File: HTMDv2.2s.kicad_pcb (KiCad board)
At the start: 2 copper layers, 90 x 49.9 mm, 105 parts, among them IC1 TJA1441AT_0Z, IC2 A3921KLPTR-T, IC3 TMP275AQDGKRQ1, J1 Conn_01x04, J10 Conn_01x02, J11 Conn_01x02, J2 Conn_01x04, J3 Conn_01x06, J4 Conn_01x01, J5 Conn_01x01_Pin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

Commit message: update
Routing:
- net SPI_SCK: track 7.98 -> 0.00 mm
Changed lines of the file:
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@@
   (segment (start 129.7262 74.1172) (end 128.6267 74.1172) (width 0.25) (layer "F.Cu") (net 4))
   (segment (start 147.075977 79.6036) (end 147.075977 64.9732) (width 0.3) (layer "F.Cu") (net 4))
-  (segment (start 130.9137 67.149546) (end 130.9137 67.9297) (width 0.25) (layer "F.Cu") (net 4))
   (segment (start 122.682 78.5876) (end 122.9614 78.867) (width 0.25) (layer "F.Cu") (net 4))
-  (segment (start 130.0988 66.334646) (end 130.9137 67.149546) (width 0.25) (layer "F.Cu") (net 4))
   (segment (start 80.935053 87.5284) (end 82.5003 87.5284) (width 0.3) (layer "F.Cu") (net 4))
   (segment (start 115.3414 79.335002) (end 115.3414 79.956401) (width 0.25) (layer "F.Cu") (net 4))
@@
   (segment (start 136.6012 70.6172) (end 137.2056 70.6172) (width 0.25) (layer "F.Cu") (net 4))
   (segment (start 147.075977 64.9732) (end 147.075977 64.4144) (width 0.3) (layer "F.Cu") (net 4))
+  (segment (start 130.0988 66.4972) (end 130.9137 67.3121) (width 0.25) (layer "F.Cu") (net 4))
   (segment (start 138.2268 69.088) (end 138.2268 68.977108) (width 0.25) (layer "F.Cu") (net 4))
   (segment (start 138.2268 68.977108) (end 138.2268 68.6308) (width 0.25) (layer "F.Cu") (net 4))
   (segment (start 122.9614 78.867) (end 122.9614 79.956401) (width 0.25) (layer "F.Cu") (net 4))
   (segment (start 122.428 78.5876) (end 122.682 78.5876) (width 0.25) (layer "F.Cu") (net 4))
-  (segment (start 130.0988 65.9373) (end 130.0988 66.334646) (width 0.25) (layer "F.Cu") (net 4))
   (segment (start 130.4137 74.8047) (end 130.4137 75.4279) (width 0.25) (layer "F.Cu") (net 4))
   (segment (start 79.756 86.349347) (end 80.935053 87.5284) (width 0.3) (layer "F.Cu") (net 4))
   (segment (start 111.517693 86.959807) (end 110.9491 87.5284) (width 0.25) (layer "F.Cu") (net 4))
   (segment (start 85.5472 86.953883) (end 85.156517 86.5632) (width 0.3) (layer "F.Cu") (net 4))
+  (segment (start 130.0988 65.9373) (end 130.0988 66.4972) (width 0.25) (layer "F.Cu") (net 4))
   (segment (start 147.075977 64.9732) (end 147.075977 55.229577) (width 0.3) (layer "F.Cu") (net 4))
   (segment (start 118.131101 78.363299) (end 116.313103 78.363299) (width 0.25) (layer "F.Cu") (net 4))
   (segment (start 122.9614 79.956401) (end 122.9614 81.3065) (width 0.25) (layer "F.Cu") (net 4))
+  (segment (start 130.9137 67.3121) (end 130.9137 67.9297) (width 0.25) (layer "F.Cu") (net 4))
   (segment (start 127.762 74.9819) (end 129.0817 74.9819) (width 0.25) (layer "F.Cu") (net 4))
   (segment (start 136.6012 69.1172) (end 137.7404 69.1172) (width 0.25) (layer "F.Cu") (net 4))
@@
   (segment (start 125.848769 71.409782) (end 128.5157 68.742851) (width 0.25) (layer "B.Cu") (net 53))
   (segment (start 125.731576 71.409782) (end 125.848769 71.409782) (width 0.25) (layer "B.Cu") (net 53))
-  (segment (start 139.4876 76.14) (end 143.743 76.14) (width 0.25) (layer "F.Cu") (net 54))
-  (segment (start 137.4648 74.1172) (end 139.4876 76.14) (width 0.25) (layer "F.Cu") (net 54))
-  (segment (start 136.6012 74.1172) (end 137.4648 74.1172) (width 0.25) (layer "F.Cu") (net 54))
   (segment (start 100.9396 85.5472) (end 100.7891 85.5472) (width 0.25) (layer "F.Cu") (net 58))
   (segment (start 99.5312 85.5472) (end 99.0448 85.0608) (width 0.25) (layer "F.Cu") (net 58))

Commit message: Update HTMDv2.2s.kicad_pcb
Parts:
- moved J9 12.9 mm to (161.6, 61.0)
- moved J3 2.64 mm to (143.7, 63.5)
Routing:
- net SWCLK: track 31.9 -> 17.3 mm
- net SWDIO: track 28.9 -> 16.3 mm
- net +3.3V: track 140.8 -> 135.6 mm
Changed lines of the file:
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@@
   )
   (footprint "Connector_PinHeader_2.54mm:PinHeader_1x04_P2.54mm_Horizontal" (layer "F.Cu")
-    (at 150.9206 53.7056)
+    (at 161.6394 60.97)
     (descr "Through hole angled pin header, 1x04, 2.54mm pitch, 6mm pin length, single row")
     (tags "Through hole angled pin header THT 1x04 2.54mm single row")
@@
   )
   (footprint "Connector_JST:JST_XH_S6B-XH-A_1x06_P2.50mm_Horizontal" (layer "B.Cu")
-    (at 143.743 66.14 -90)
+    (at 143.7176 63.4968 -90)
     (descr "JST XH series connector, S6B-XH-A (http://www.jst-mfg.com/product/pdf/eng/eXH.pdf), generated with kicad-footprint-generator")
     (tags "connector JST XH horizontal")
@@
   (gr_line (start 66.5 39) (end 150.5 39)
     (stroke (width 0.1) (type default)) (layer "Edge.Cuts"))
-  (gr_text "ENCODER" (at 152.7048 74.5236 90) (layer "F.SilkS")
+  (gr_text "ENCODER" (at 152.1968 71.9328 90) (layer "F.SilkS")
     (effects (font (size 1 1) (thickness 0.2) bold) (justify left bottom))
   )
@@
   (segment (start 109.008206 88.623) (end 77.7703 88.623) (width 0.3) (layer "B.Cu") (net 3))
   (segment (start 77.7703 88.623) (end 77.5208 88.3735) (width 0.3) (layer "B.Cu") (net 3))
-  (segment (start 150.164777 61.3256) (end 150.9206 61.3256) (width 0.3) (layer "F.Cu") (net 4))
   (segment (start 128.6267 74.1172) (end 127.762 74.9819) (width 0.25) (layer "F.Cu") (net 4))
   (segment (start 122.9614 81.3065) (end 123.7488 82.0939) (width 0.25) (layer "F.Cu") (net 4))
@@
   (segment (start 136.6012 69.1172) (end 137.7404 69.1172) (width 0.25) (layer "F.Cu") (net 4))
   (segment (start 136.6012 70.1172) (end 137.1976 70.1172) (width 0.25) (layer "F.Cu") (net 4))
-  (segment (start 147.075977 64.4144) (end 150.164777 61.3256) (width 0.3) (layer "F.Cu") (net 4))
   (via (at 111.755368 86.959807) (size 0.8) (drill 0.4) (layers "F.Cu" "B.Cu") (net 4))
   (via (at 129.4892 87.0712) (size 0.8) (drill 0.4) (layers "F.Cu" "B.Cu") (net 4))
@@
   (via (at 128.9657 65.0748) (size 0.8) (drill 0.4) (layers "F.Cu" "B.Cu") (net 43))
   (segment (start 128.9657 65.0748) (end 129.5245 64.516) (width 0.25) (layer "B.Cu") (net 43))
-  (segment (start 146.476996 58.7856) (end 150.9206 58.7856) (width 0.25) (layer "B.Cu") (net 43))
-  (segment (start 140.746596 64.516) (end 146.476996 58.7856) (width 0.25) (layer "B.Cu") (net 43))
   (segment (start 129.5245 64.516) (end 140.746596 64.516) (width 0.25) (layer "B.Cu") (net 43))
   (segment (start 129.4231 68.6172) (end 129.7262 68.6172) (width 0.25) (layer "F.Cu") (net 44))
@@
   (segment (start 128.876893 64.079251) (end 128.890144 64.066) (width 0.25) (layer "B.Cu") (net 44))
   (segment (start 128.890144 64.066) (end 140.5602 64.066) (width 0.25) (layer "B.Cu") (net 44))
-  (segment (start 140.5602 64.066) (end 150.9206 53.7056) (width 0.25) (layer "B.Cu") (net 44))
   (segment (start 95.4024 87.9845) (end 93.7252 87.9845) (width 0.3) (layer "F.Cu") (net 45))
   (segment (start 93.6752 88.0345) (end 91.948 88.0345) (width 0.3) (layer "F.Cu") (net 45))

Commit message: update
add power line
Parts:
- moved J3 8.79 mm to (144.0, 54.7)
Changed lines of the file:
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@@
   )
   (footprint "Connector_JST:JST_XH_S6B-XH-A_1x06_P2.50mm_Horizontal" (layer "B.Cu")
-    (at 143.7176 63.4968 -90)
+    (at 143.9716 54.71 -90)
     (descr "JST XH series connector, S6B-XH-A (http://www.jst-mfg.com/product/pdf/eng/eXH.pdf), generated with kicad-footprint-generator")
     (tags "connector JST XH horizontal")
@@
   (segment (start 126.8912 56.969188) (end 126.6152 56.693188) (width 0.25) (layer "F.Cu") (net 88))
   (segment (start 129.7262 72.1172) (end 128.224016 72.1172) (width 0.25) (layer "F.Cu") (net 90))
-  (segment (start 119.871196 51.2136) (end 112.0212 51.2136) (width 0.25) (layer "F.Cu") (net 90))
-  (segment (start 112.0212 51.2136) (end 110.0836 49.276) (width 0.25) (layer "F.Cu") (net 90))
+  (segment (start 108.5088 43.8912) (end 107.235 43.8912) (width 0.25) (layer "F.Cu") (net 90))
+  (segment (start 125.9912 57.34198) (end 125.7152 57.06598) (width 0.25) (layer "F.Cu") (net 90))
+  (segment (start 125.7152 57.06598) (end 125.7152 57.057604) (width 0.25) (layer "F.Cu") (net 90))
+  (segment (start 110.8456 46.228) (end 108.5088 43.8912) (width 0.25) (layer "F.Cu") (net 90))
+  (segment (start 125.7152 57.057604) (end 119.871196 51.2136) (width 0.25) (layer "F.Cu") (net 90))
+  (segment (start 113.0372 51.2136) (end 110.8456 49.022) (width 0.25) (layer "F.Cu") (net 90))
   (segment (start 128.224016 72.1172) (end 125.9912 69.884384) (width 0.25) (layer "F.Cu") (net 90))
-  (segment (start 125.9912 57.34198) (end 125.7152 57.06598) (width 0.25) (layer "F.Cu") (net 90))
+  (segment (start 119.871196 51.2136) (end 113.0372 51.2136) (width 0.25) (layer "F.Cu") (net 90))
   (segment (start 125.9912 69.884384) (end 125.9912 57.34198) (width 0.25) (layer "F.Cu") (net 90))
-  (segment (start 108.0008 43.8912) (end 107.235 43.8912) (width 0.25) (layer "F.Cu") (net 90))
-  (segment (start 110.0836 49.276) (end 110.0836 45.974) (width 0.25) (layer "F.Cu") (net 90))
-  (segment (start 125.7152 57.06598) (end 125.7152 57.057604) (width 0.25) (layer "F.Cu") (net 90))
-  (segment (start 110.0836 45.974) (end 108.0008 43.8912) (width 0.25) (layer "F.Cu") (net 90))
-  (segment (start 125.7152 57.057604) (end 119.871196 51.2136) (width 0.25) (layer "F.Cu") (net 90))
+  (segment (start 110.8456 49.022) (end 110.8456 46.228) (width 0.25) (layer "F.Cu") (net 90))
   (segment (start 129.3368 80.1605) (end 129.2371 80.1605) (width 0.25) (layer "F.Cu") (net 91))
   (segment (start 127.254 82.1436) (end 127.254 84.6722) (width 0.25) (layer "F.Cu") (net 91))

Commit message: update
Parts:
- removed D1: D, 0-Myparts:SS2040FL
- added C24: 4.7u, Capacitor_SMD:C_0603_1608Metric_Pad1.08x0.95mm_HandSolder, F.Cu at (136.2, 53.6)
- added C25: C, Capacitor_SMD:C_0603_1608Metric_Pad1.08x0.95mm_HandSolder, F.Cu at (137.1, 60.5)
- added C28: 10u, Capacitor_SMD:C_0805_2012Metric_Pad1.18x1.45mm_HandSolder, F.Cu at (139.1, 63.3)
- added C29: 10u, Capacitor_SMD:C_0805_2012Metric_Pad1.18x1.45mm_HandSolder, F.Cu at (135.3, 63.3)
- added L1: 4.7u, Inductor_SMD:L_0603_1608Metric_Pad1.05x0.95mm_HandSolder, F.Cu at (140.2, 60.5)
- added R39: R, Resistor_SMD:R_0603_1608Metric_Pad0.98x0.95mm_HandSolder, F.Cu at (138.6, 60.5)
- added R40: R, Resistor_SMD:R_0603_1608Metric_Pad0.98x0.95mm_HandSolder, F.Cu at (134.3, 57.1)
- added R41: 100k, Inductor_SMD:L_0603_1608Metric_Pad1.05x0.95mm_HandSolder, F.Cu at (137.1, 57.1)
- C2, C3: value 1u -> 10u; footprint Capacitor_SMD:C_0603_1608Metric_Pad1.08x0.95mm_HandSolder -> Capacitor_SMD:C_0805_2012Metric_Pad1.18x1.45mm_HandSolder
- U1: value ADP3338AKCZ-3.3 -> TPS628511DRLR; footprint 0-Myparts:SOT230P700X180-4N -> 0_Mylib:DRL0008A-MFG
- moved C3 71.9 mm to (139.0, 52.2), turned to 180 degrees
- moved C2 53.6 mm to (139.0, 54.3), turned to 180 degrees
- moved U1 40.7 mm to (139.4, 56.9)
- moved C12 3.32 mm to (138.6, 70.7), turned to -90 degrees
- moved C9 2.34 mm to (134.3, 53.6), turned to 90 degrees
- moved C19 0.87 mm to (134.3, 60.6)
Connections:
- C3 pad 1: +3.3V -> VCC
- U1 pad 1: GND -> VCC
- U1 pad 2: +3.3V -> VCC
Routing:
- net +3.3V: track 135.6 -> 110.4 mm
- net VCC: track 138.8 -> 118.2 mm
- net Net-(U1-FB): track 0.00 -> 6.99 mm
- net Net-(U1-PG): track 0.00 -> 3.43 mm
- net Net-(U1-SS_TR): track 0.00 -> 3.10 mm
- net Net-(U1-SW): track 0.00 -> 2.24 mm
- added copper zone on F.Cu, net +3.3V
- added copper zone on F.Cu, net VCC

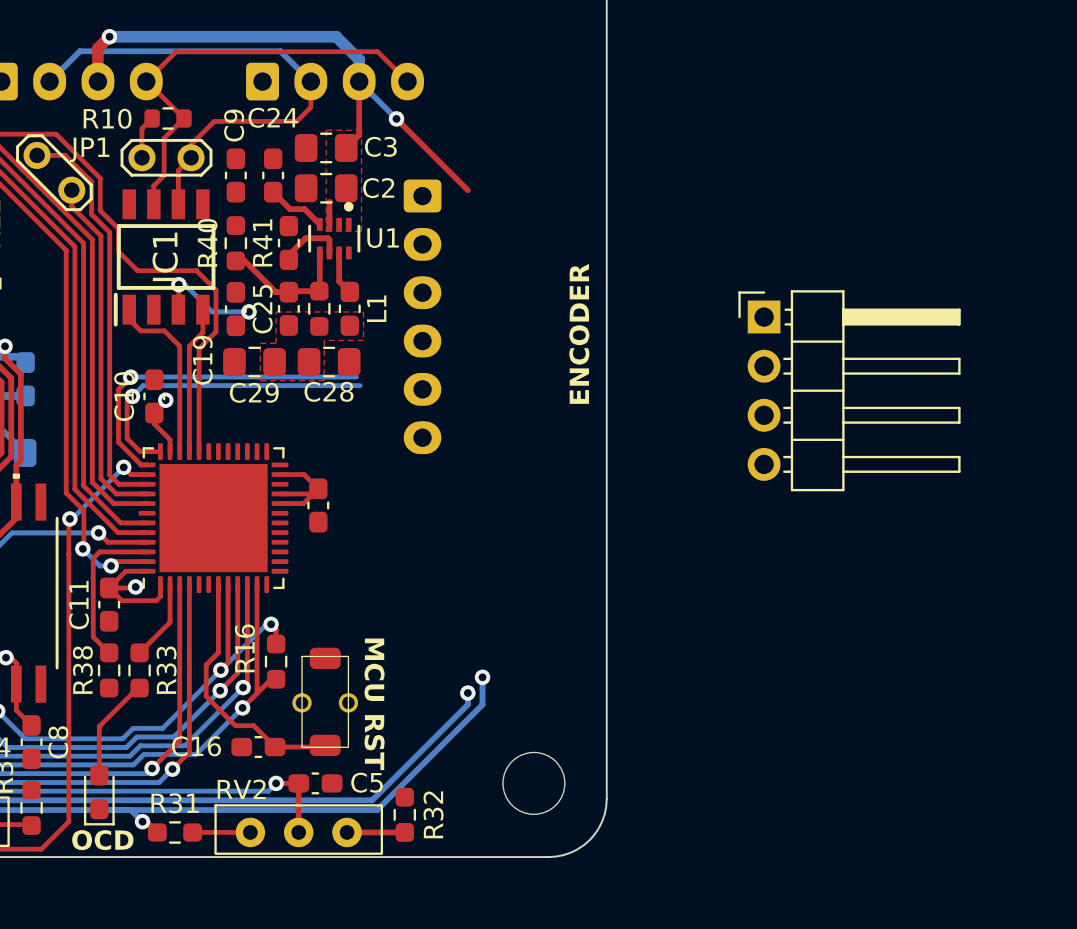
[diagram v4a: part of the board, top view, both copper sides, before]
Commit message: update
SYS配線の見直し
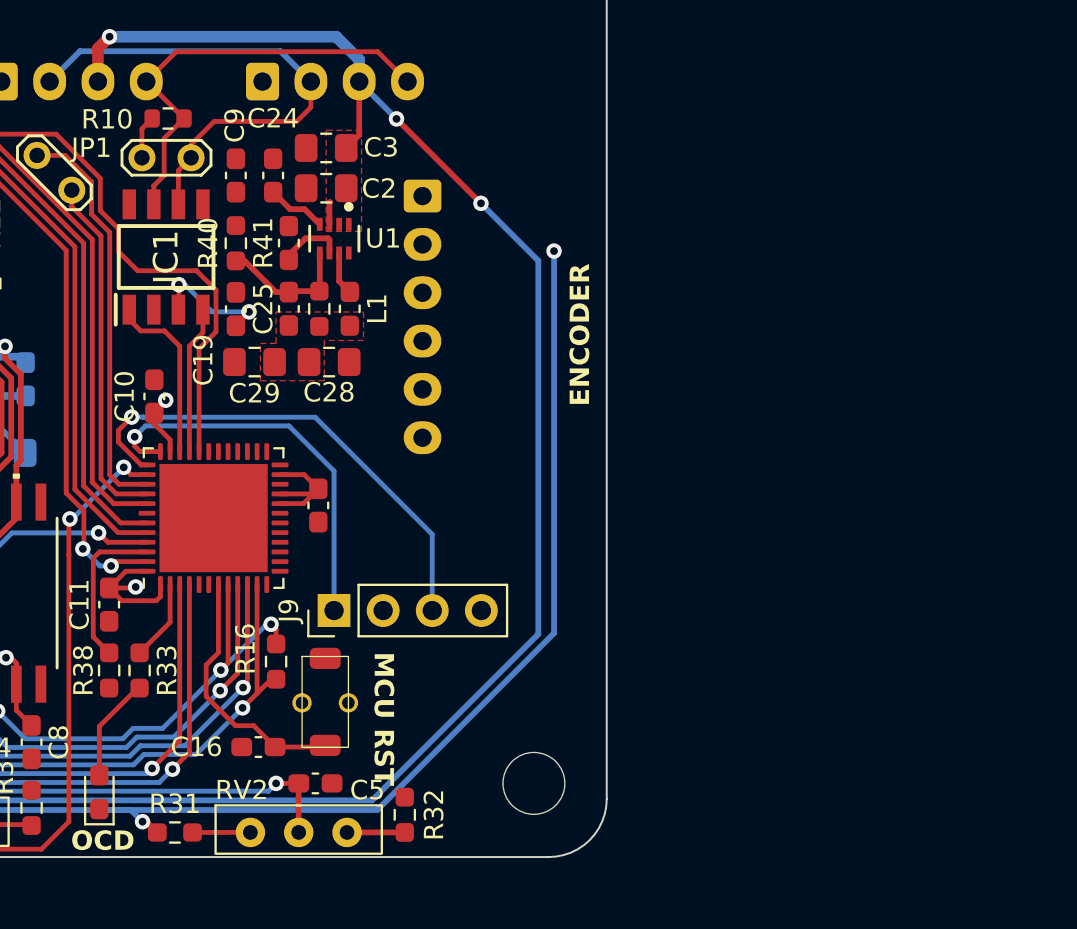
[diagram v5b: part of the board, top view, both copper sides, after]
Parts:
- J9: footprint Connector_PinHeader_2.54mm:PinHeader_1x04_P2.54mm_Horizontal -> Connector_PinHeader_2.54mm:PinHeader_1x04_P2.54mm_Vertical
- moved J9 26.9 mm to (139.4, 76.1), turned to 90 degrees
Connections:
- J9 pad 1: SWCLK -> SWDIO
- J9 pad 3: SWDIO -> SWCLK
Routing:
- net VCC: track 118.2 -> 147.3 mm
- net +3.3V: track 110.4 -> 133.9 mm
- net SWCLK: track 17.3 -> 25.6 mm
- net SWDIO: track 16.3 -> 20.7 mm

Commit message: pre cmpl
レビューまち
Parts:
- added D1: LED, LED_SMD:LED_0603_1608Metric_Pad1.05x0.95mm_HandSolder, F.Cu at (151.6, 71.2)
- added D7: LED, LED_SMD:LED_0603_1608Metric_Pad1.05x0.95mm_HandSolder, F.Cu at (151.6, 73.9)
- added D8: LED, LED_SMD:LED_0603_1608Metric_Pad1.05x0.95mm_HandSolder, F.Cu at (151.6, 76.7)
- added D9: LED, LED_SMD:LED_0603_1608Metric_Pad1.05x0.95mm_HandSolder, F.Cu at (151.5, 79.4)
- added R42: R, Resistor_SMD:R_0603_1608Metric_Pad0.98x0.95mm_HandSolder, F.Cu at (147.2, 71.2)
- added R43: R, Resistor_SMD:R_0603_1608Metric_Pad0.98x0.95mm_HandSolder, F.Cu at (147.2, 72.7)
- added R44: R, Resistor_SMD:R_0603_1608Metric_Pad0.98x0.95mm_HandSolder, F.Cu at (147.2, 74.2)
- added R45: R, Resistor_SMD:R_0603_1608Metric_Pad0.98x0.95mm_HandSolder, F.Cu at (147.2, 75.7)
- JP2, JP3, JP4, JP5: footprint Jumper:SolderJumper-2_P1.3mm_Open_TrianglePad1.0x1.5mm -> Resistor_SMD:R_0603_1608Metric_Pad0.98x0.95mm_HandSolder
- moved R30 140.3 mm to (91.2, 61.3), turned to 180 degrees
- moved JP5 111.8 mm to (146.5, 66.8), turned to -90 degrees
- moved D6 57.7 mm to (151.7, 50.9), turned to 180 degrees
- moved R37 54.3 mm to (148.2, 50.9)
- moved JP3 41.5 mm to (151.2, 66.8), turned to -90 degrees
- moved JP2 40.4 mm to (149.6, 66.8), turned to -90 degrees
- moved JP4 39.6 mm to (148.0, 66.8), turned to -90 degrees
- moved SW2 2.99 mm to (141.2, 82.9), turned to -90 degrees
- moved J9 2.31 mm to (139.0, 78.4)
- moved C12 1.19 mm to (139.7, 71.1), turned to 0 degrees
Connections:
- JP2 pad 1: Net-(J3-Pin_3) -> Net-(J3-Pin_1)
- JP2 pad 2: ENC_B -> SPI_MOSI
- JP5 pad 1: Net-(J3-Pin_1) -> Net-(J3-Pin_3)
- JP5 pad 2: SPI_MOSI -> ENC_B
- R37 pad 1: unconnected-(R37-Pad1) -> LED1
- U2 pad 13: SPI_SCK -> LED5
- U2 pad 14: SPI_MISO -> unconnected-(U2-PA6-Pad14)
- U2 pad 15: SPI_MOSI -> unconnected-(U2-PA7-Pad15)
- U2 pad 16: SPI_CS -> unconnected-(U2-PC4-Pad16)
- U2 pad 17: unconnected-(U2-PB0-Pad17) -> LED4
- U2 pad 18: unconnected-(U2-PB1-Pad18) -> LED3
- U2 pad 19: unconnected-(U2-PB2-Pad19) -> LED2
- U2 pad 24: unconnected-(U2-PB11-Pad24) -> LED1
- U2 pad 25: LED5 -> SPI_CS
- U2 pad 26: LED4 -> SPI_SCK
- U2 pad 27: LED3 -> SPI_MISO
- U2 pad 28: LED2 -> SPI_MOSI
- U2 pad 29: LED1 -> unconnected-(U2-PC6-Pad29)
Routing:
- net +3.3V: track 133.9 -> 235.1 mm, vias 8 -> 17
- net LED1: track 0.00 -> 28.8 mm, vias 0 -> 2
- net GND: track 85.2 -> 110.1 mm, vias 2 -> 42
- net SPI_MISO: track 0.00 -> 20.2 mm
- net SPI_MOSI: track 0.00 -> 19.2 mm
- net VCC: track 147.3 -> 166.2 mm
- net ENC_A: track 0.00 -> 18.4 mm
- net ENC_B: track 0.00 -> 17.4 mm
- net Net-(J3-Pin_1): track 0.00 -> 16.2 mm
- net Net-(J3-Pin_3): track 0.00 -> 13.4 mm
- net SPI_SCK: track 0.00 -> 11.9 mm, vias 0 -> 1
- net LED2: track 0.00 -> 10.6 mm
- net LED4: track 0.00 -> 10.5 mm
- net SPI_CS: track 0.00 -> 10.5 mm, vias 0 -> 1
- net LED5: track 0.00 -> 10.3 mm
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- added copper zone on B.Cu, net GND
- added copper zone on F.Cu, net GND
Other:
- board text added: "ENC A"
- board text added: "ENC B"
- board text added: "SPI_MISO"
- board text added: "SPI_MOSI"
- board text added: "Tx Rx"
